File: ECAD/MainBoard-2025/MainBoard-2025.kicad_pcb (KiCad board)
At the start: 2 copper layers, 100 x 100 mm, 142 parts, among them J1 XT60, J10 Conn_01x02, J11 Conn_01x04, J12 Conn_01x04, J15 Conn_01x02, J16 XT30, J18 Conn_01x02, J2 Conn_01x04, J20 BAU, J21 BAU, J22 Conn_01x04, J23 Conn_01x02, J26 BAU, J28 Conn_01x02, J29 Conn_01x02, J3 Conn_01x04, J4 Conn_01x02, J7 XT30, J8 Conn_01x02, J9 Conn_01x02, K2 FINDER-36.11, U2 R-78B3.3-2.0, U3 R-78B12-2.0, U4 R-78B5.0-2.0, U5 Teensy4.1

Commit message: new board cut edge and new robot frames
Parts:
- removed the G*** at (134.0, 60.0)
- C1, C2, C7, D10, D11, D3, D8, IHM-IO2, J3, R17, R2, R5, R7, U2, U3, U4, USB-Prog1: moved to B.Cu
- D2, D7, D9: moved to F.Cu
- moved G*** 257.8 mm to (-34.1, 29.8)
- moved G*** 257.8 mm to (-81.2, -23.8)
- moved G*** 257.8 mm to (-34.1, 21.7)
- moved kibuzzard-64932EB2 257.8 mm to (-60.0, -57.8)
- moved kibuzzard-64933136 257.8 mm to (-61.2, -2.69)
- moved kibuzzard-64933140 257.8 mm to (-61.2, -28.1)
- moved kibuzzard-64944D19 257.8 mm to (-60.0, -34.8)
- moved kibuzzard-64944D37 257.8 mm to (-41.7, 21.5)
- moved G*** 257.8 mm to (-115.6, 20.7)
- moved G*** 257.8 mm to (-42.2, -55.8)
- moved G*** 257.8 mm to (-75.5, 0.62)
- moved G*** 257.8 mm to (-120.4, -22.6)
- moved G*** 257.8 mm to (-62.6, -34.2)
- moved G*** 257.8 mm to (-125.3, 22.5)
- moved G*** 257.8 mm to (-42.2, -44.1)
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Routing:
- net +5V: track 182.3 -> 0.00 mm
- net +3V3: track 75.4 -> 0.00 mm
- net +24V: track 58.9 -> 0.00 mm
- net +12V: track 58.1 -> 0.00 mm
- net Net-(D4-A): track 17.9 -> 0.00 mm
- net +BATT: track 6.82 -> 0.00 mm
- net /24VD: track 5.79 -> 0.00 mm
- net SCL: track 4.73 -> 0.00 mm
- net SDA: track 3.02 -> 0.00 mm
- net Net-(Con-TFT1-Pin_1): track 2.80 -> 0.00 mm
- net Net-(D1-A): track 2.68 -> 0.00 mm
- net Net-(D10-A): track 2.55 -> 0.00 mm
- net Net-(D8-A): track 2.42 -> 0.00 mm
- net Net-(D5-A): track 2.30 -> 0.00 mm
- net Net-(D6-A): track 2.18 -> 0.00 mm
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- removed copper zone on F.Cu, net +24V
- removed copper zone on B.Cu, net +5VP
- removed copper zone on B.Cu, net +BATT
- removed copper zone on F.Cu, net +BATT
- removed copper zone on B.Cu, net /24VD
- removed copper zone on F.Cu, net /24VD
- removed copper zone on B.Cu, net GND
- removed copper zone on F.Cu, net GND
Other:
- board size 100 x 100 mm -> 60 x 168.7 mm
- board text removed: "! USB PROGRAMMING ! ! CABLE !"

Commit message: wire power side
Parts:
- C1, C2, C7, D10, D3, D8, R17, R2, R5: moved to F.Cu
- C6: moved to B.Cu
- moved C6 131.5 mm to (105.4, 224.8), turned to 90 degrees
- moved D3 47.3 mm to (99.5, 194.0), turned to 90 degrees
- moved D10 40.0 mm to (93.5, 194.0), turned to 90 degrees
- moved R2 39.5 mm to (99.5, 188.0), turned to 90 degrees
- moved D8 39.5 mm to (102.5, 194.0), turned to 90 degrees
- moved R5 33.3 mm to (93.5, 188.0), turned to 90 degrees
- moved R17 33.2 mm to (102.5, 188.0), turned to 90 degrees
- moved J21 27.2 mm to (115.9, 219.0), turned to 90 degrees
- moved D6 27.1 mm to (96.5, 194.0), turned to 90 degrees
- moved R4 26.9 mm to (96.5, 188.0), turned to 90 degrees
- moved R3 24.0 mm to (87.5, 188.0)
- moved D5 23.5 mm to (87.5, 194.0)
- moved R1 21.3 mm to (90.5, 188.0)
- moved D1 21.1 mm to (90.5, 194.0)
- moved J20 16.8 mm to (82.0, 224.9), turned to 90 degrees
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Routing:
- net +24V: track 0.00 -> 121.9 mm
- net +5VP: track 0.00 -> 93.4 mm, vias 0 -> 1
- net +12V: track 0.00 -> 90.7 mm, vias 0 -> 1
- net +5V: track 0.00 -> 81.4 mm, vias 0 -> 1
- net Net-(D4-A): track 0.00 -> 35.7 mm
- net +3V3: track 0.00 -> 22.6 mm, vias 0 -> 1
- net +BATT: track 0.00 -> 22.2 mm
- net /24VD: track 0.00 -> 3.40 mm
- net Net-(D8-A): track 0.00 -> 2.96 mm
- net Net-(D6-A): track 0.00 -> 2.96 mm
- net Net-(D5-A): track 0.00 -> 2.96 mm
- net Net-(D3-A): track 0.00 -> 2.96 mm
- net Net-(D10-A): track 0.00 -> 2.96 mm
- net Net-(D1-A): track 0.00 -> 2.96 mm
- added copper zone on B.Cu, net +24V
- added copper zone on F.Cu, net +24V
- added copper zone on B.Cu, net +BATT
- added copper zone on F.Cu, net +BATT
- added copper zone on B.Cu, net /24VD
- added copper zone on F.Cu, net /24VD
- added copper zone on B.Cu, net GND
- added copper zone on F.Cu, net GND
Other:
- board size 60 x 168.7 mm -> 56 x 169 mm

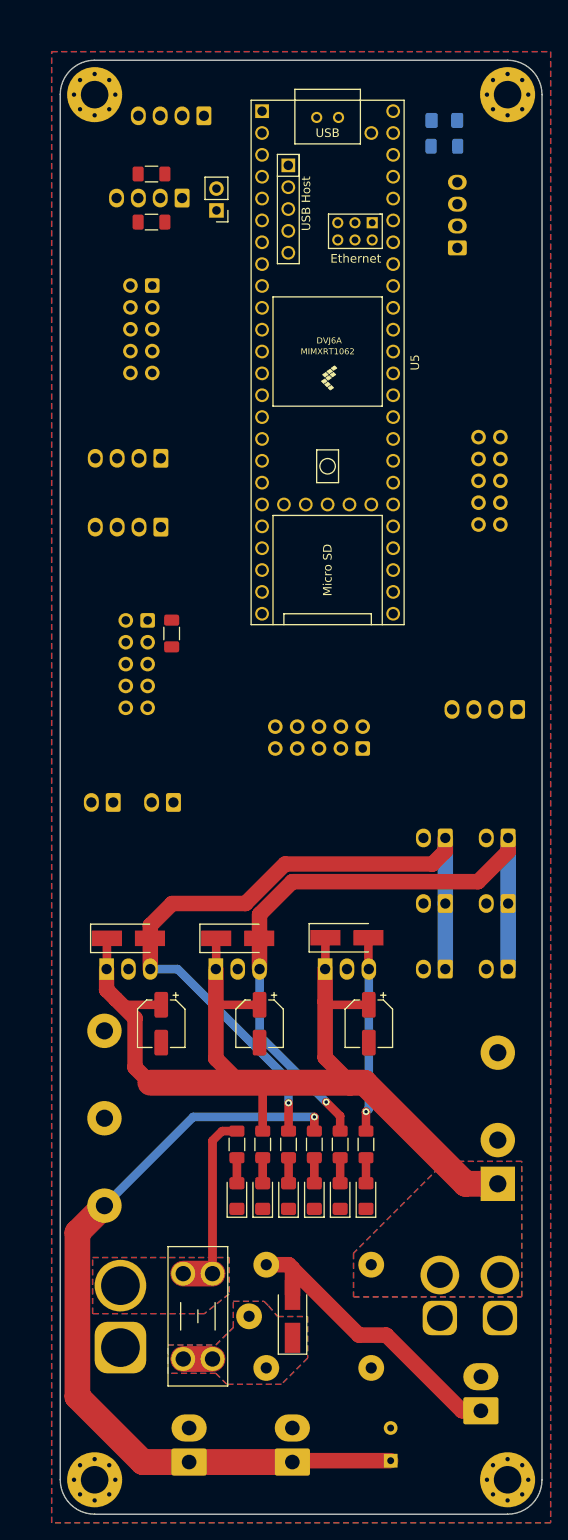
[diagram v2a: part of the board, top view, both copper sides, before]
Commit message: Change board size - Move uC - Add connector for Otos sensor
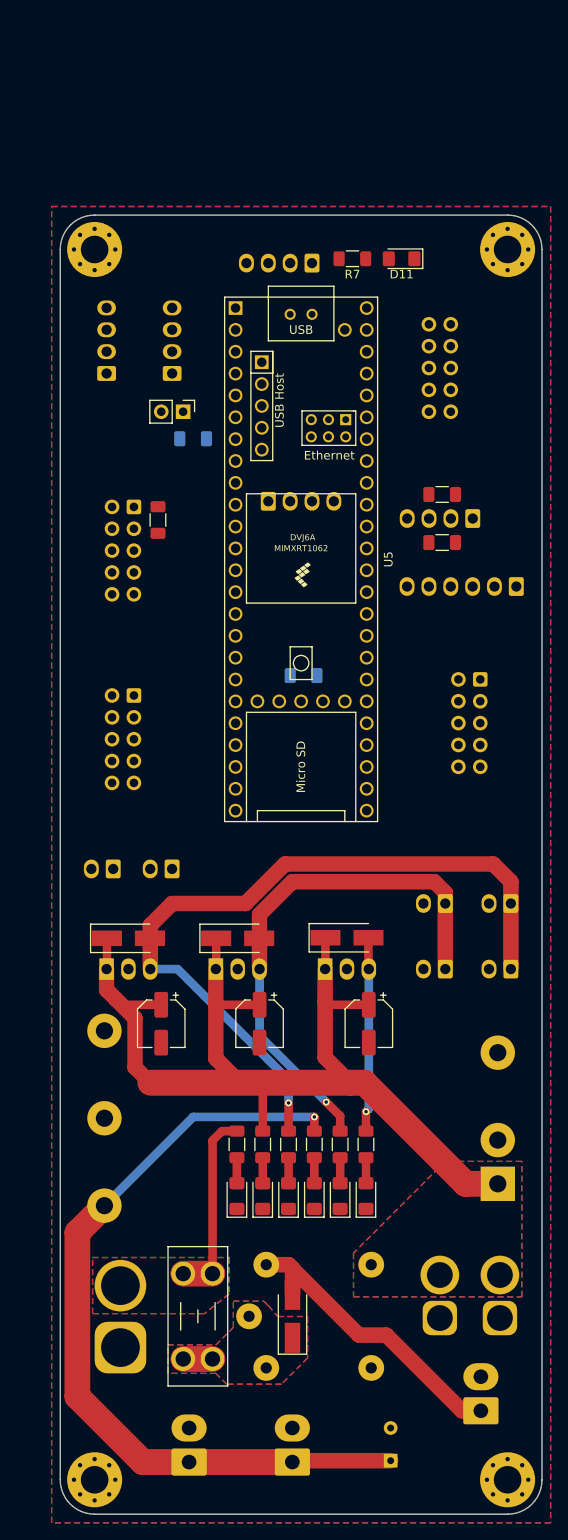
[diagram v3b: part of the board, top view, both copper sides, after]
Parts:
- removed J10, J29: Conn_01x02, Connector_Molex:Molex_KK-254_AE-6410-02A_1x02_P2.54mm_Vertical
- removed J3: Conn_01x04, Connector_Molex:Molex_KK-254_AE-6410-04A_1x04_P2.54mm_Vertical
- added J6: Conn_01x06, Connector_Molex:Molex_KK-254_AE-6410-06A_1x06_P2.54mm_Vertical, B.Cu at (120.0, 123.2)
- added R8: 100, Resistor_SMD:R_1206_3216Metric_Pad1.30x1.75mm_HandSolder, B.Cu at (95.3, 133.5)
- added R9: 100, Resistor_SMD:R_1206_3216Metric_Pad1.30x1.75mm_HandSolder, B.Cu at (82.5, 106.0)
- D11, R7: moved to F.Cu
- moved R21 50.3 mm to (111.4, 112.5)
- moved J22 50.3 mm to (115.0, 115.3)
- moved R22 50.3 mm to (111.4, 118.1)
- moved IHM-IO2 47.7 mm to (75.6, 135.8)
- moved J12 30.2 mm to (80.0, 98.4), turned to 90 degrees
- moved J8 23.7 mm to (81.3, 102.9), turned to -90 degrees
- moved U5 23.1 mm to (95.0, 120.0)
- moved H1 18.0 mm to (71.0, 84.0)
- moved H2 18.0 mm to (119.0, 84.0)
- moved USB-Prog1 17.0 mm to (96.3, 85.6), turned to 180 degrees
- moved R7 16.9 mm to (101.0, 85.1)
- moved D11 16.8 mm to (106.7, 85.1)
- moved IHM-IO1 15.8 mm to (115.8, 134.0), turned to 180 degrees
- moved C_Act1 14.3 mm to (112.4, 92.7)
- moved Con-TFT1 13.3 mm to (75.6, 113.9)
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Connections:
- J22 pad 3: +5V -> +3V3
- R21 pad 2: +5V -> +3V3
- R22 pad 2: +5V -> +3V3
- U5 pad 5: unconnected-(U5-3_LRCLK2-Pad5) -> Net-(U5-3_LRCLK2)
- U5 pad 51: unconnected-(U5-3V3-Pad51) -> Net-(R8-Pad2)
- U5 pad 53: unconnected-(U5-PROGRAM-Pad53) -> Net-(U5-PROGRAM)
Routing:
- net +5V: track 81.4 -> 65.3 mm
- net +12V: track 90.7 -> 91.9 mm
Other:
- board size 56 x 169 mm -> 56 x 151 mm

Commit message: Power all the components
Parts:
- removed J11: Conn_01x04, Connector_Molex:Molex_KK-254_AE-6410-04A_1x04_P2.54mm_Vertical
- added BZ1: Buzzer, Buzzer_Beeper:Buzzer_15x7.5RM7.6, F.Cu at (79.8, 99.1)
- added C3: 100uF, Capacitor_SMD:CP_Elec_5x5.4, B.Cu at (76.0, 102.8)
- added JP1: SolderJumper_2_Open, Jumper:SolderJumper-2_P1.3mm_Open_RoundedPad1.0x1.5mm, B.Cu at (83.3, 99.8)
- added JP2: SolderJumper_2_Open, Jumper:SolderJumper-2_P1.3mm_Open_RoundedPad1.0x1.5mm, B.Cu at (83.3, 96.8)
- R9: value 100 -> 330
- moved J2 29.3 mm to (91.2, 121.0), turned to 0 degrees
- moved J12 20.3 mm to (95.5, 85.3), turned to 180 degrees
- moved USB-Prog1 13.0 mm to (109.2, 85.3)
- moved J8 11.7 mm to (83.8, 91.4), turned to 180 degrees
- moved J18 5.37 mm to (78.5, 155.4)
- moved J15 5.37 mm to (85.3, 155.4)
- moved C_Act1 4.56 mm to (116.3, 95.0)
- moved R9 3.24 mm to (82.5, 102.8)
- moved D11 3.15 mm to (108.2, 82.3)
- moved R7 3.15 mm to (102.5, 82.3)
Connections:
- net Net-(U5-3_LRCLK2) renamed Buzzer
- U5 pad 56: D- Host -> unconnected-(U5-D--Pad56)
- U5 pad 57: D+ Host -> unconnected-(U5-D+-Pad57)
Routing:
- net +5V: track 65.3 -> 247.6 mm
- net +3V3: track 22.6 -> 183.3 mm
- net /vusb: track 0.00 -> 4.65 mm
- net Net-(D11-A): track 0.00 -> 2.68 mm

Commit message: Routing ok - Just before Silkscreen
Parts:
- moved R6 6.05 mm to (74.0, 111.2), turned to 0 degrees
- moved R8 0.28 mm to (95.0, 133.5)
- turned JP2 to 180 degrees
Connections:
- U5 pad 17: DIR_1 -> DIR_2
- U5 pad 18: DIR_2 -> DIR_3
- U5 pad 19: DIR_3 -> STEP_2
- U5 pad 6: STEP_1 -> DIR_1
- U5 pad 7: STEP_2 -> STEP_3
- U5 pad 8: STEP_3 -> STEP_1
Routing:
- net En5VP: track 0.00 -> 70.5 mm, vias 0 -> 1
- net Couleur: track 0.00 -> 50.9 mm, vias 0 -> 1
- net Detection: track 0.00 -> 50.8 mm
- net C_Act1-6: track 0.00 -> 45.0 mm
- net STEP_3: track 0.00 -> 41.6 mm
- net DIR_1: track 0.00 -> 38.2 mm
- net STEP_1: track 0.00 -> 38.1 mm
- net TX-loc: track 0.00 -> 36.9 mm, vias 0 -> 1
- net C_Act1-3: track 0.00 -> 34.6 mm, vias 0 -> 1
- net C_Act1-8: track 0.00 -> 34.5 mm
- net TFT_SCK: track 0.00 -> 32.9 mm, vias 0 -> 1
- net RX-loc: track 0.00 -> 32.7 mm, vias 0 -> 1
- net C_Act1-9: track 0.00 -> 28.6 mm, vias 0 -> 1
- net SCL: track 0.00 -> 28.0 mm
- net C_Act1-5: track 0.00 -> 25.0 mm, vias 0 -> 1
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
